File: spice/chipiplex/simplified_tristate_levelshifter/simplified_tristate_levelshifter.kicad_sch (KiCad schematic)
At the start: 24 parts, among them Q1 PNP, Q2 NPN, Q3 PNP, Q4 NPN

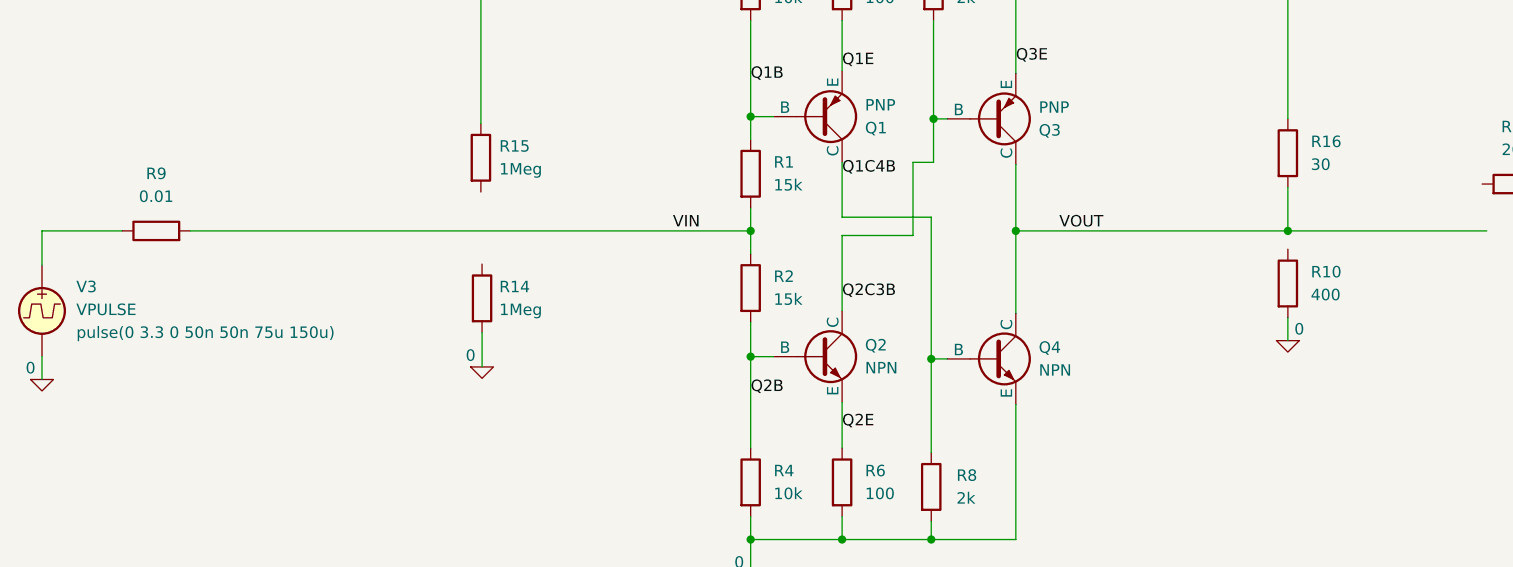
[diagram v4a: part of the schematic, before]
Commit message: Added finalized production files for v0.1r1.
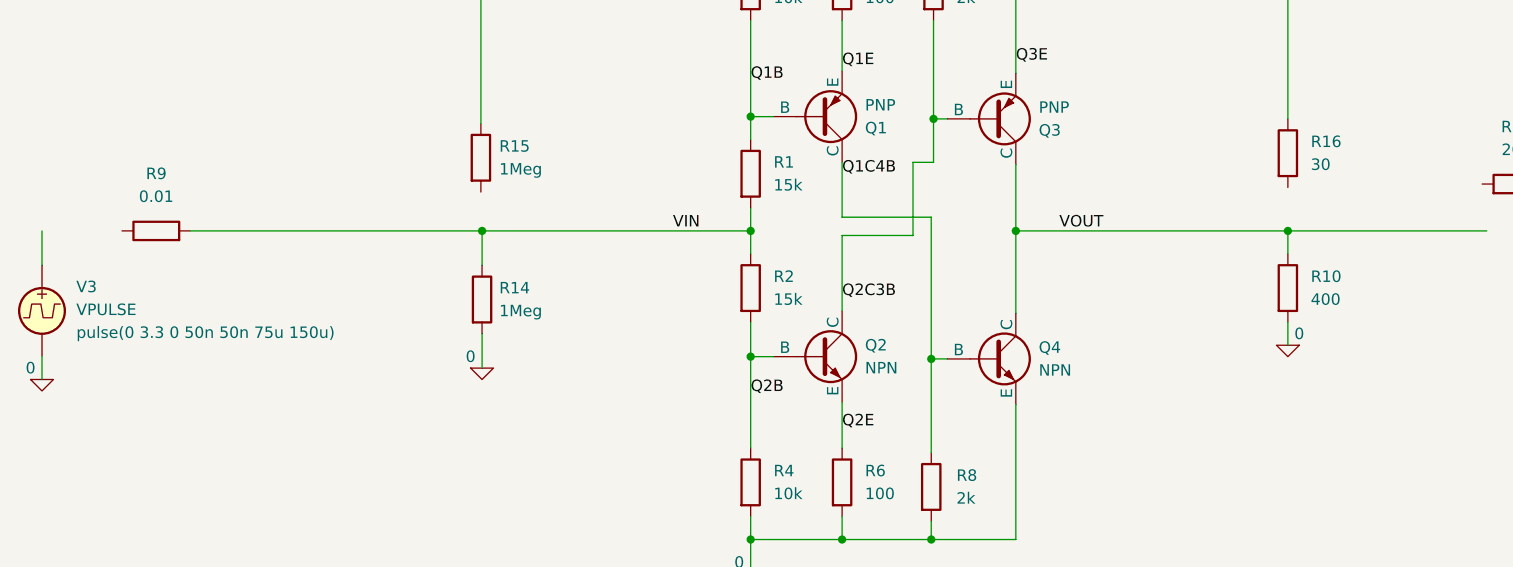
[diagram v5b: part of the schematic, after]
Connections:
- net VIN: now also R14.1
- net VOUT: now also R10.1; no longer R16.2
- net at R9.1: no longer V3.1
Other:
- moved on the sheet: R10
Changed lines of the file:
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@@
   (junction (at 124.206 130.81) (diameter 0) (color 0 0 0 0)
   )
+  (junction (at 133.604 96.52) (diameter 0) (color 0 0 0 0)
+  )
   (junction (at 163.83 96.52) (diameter 0) (color 0 0 0 0)
   )
-  (junction (at 133.604 96.52) (diameter 0) (color 0 0 0 0)
-  )
   (junction (at 104.14 96.52) (diameter 0) (color 0 0 0 0)
   )
@@
   (junction (at 124.206 110.744) (diameter 0) (color 0 0 0 0)
   )
+  (junction (at 74.295 96.52) (diameter 0) (color 0 0 0 0)
+  )
   (junction (at 114.3 130.81) (diameter 0) (color 0 0 0 0)
   )
@@
   (junction (at 104.267 62.738) (diameter 0) (color 0 0 0 0)
   )
+  (wire (pts (xy 74.295 96.52) (xy 104.14 96.52))
+    (stroke (width 0) (type default))
+  )
+  (wire (pts (xy 163.83 96.52) (xy 185.928 96.52))
+    (stroke (width 0) (type default))
+  )
   (wire (pts (xy 104.14 106.68) (xy 104.14 110.49))
     (stroke (width 0) (type default))
@@
     (stroke (width 0) (type default))
   )
-  (wire (pts (xy 74.295 107.823) (xy 74.295 111.633))
+  (wire (pts (xy 74.295 107.95) (xy 74.295 111.76))
     (stroke (width 0) (type default))
   )
@@
     (stroke (width 0) (type default))
   )
+  (wire (pts (xy 163.83 96.52) (xy 163.83 99.06))
+    (stroke (width 0) (type default))
+  )
   (wire (pts (xy 114.3 97.028) (xy 114.3 105.41))
     (stroke (width 0) (type default))
@@
     (stroke (width 0) (type default))
   )
+  (wire (pts (xy 74.295 96.52) (xy 74.295 100.33))
+    (stroke (width 0) (type default))
+  )
   (wire (pts (xy 133.604 115.824) (xy 133.604 130.81))
     (stroke (width 0) (type default))
@@
     (stroke (width 0) (type default))
   )
-  (wire (pts (xy 163.83 96.52) (xy 185.928 96.52))
-    (stroke (width 0) (type default))
-  )
-  (wire (pts (xy 41.91 96.52) (xy 104.14 96.52))
-    (stroke (width 0) (type default))
-  )
-  (wire (pts (xy 163.83 106.172) (xy 163.83 108.712))
-    (stroke (width 0) (type default))
-  )
-  (wire (pts (xy 25.4 96.52) (xy 34.29 96.52))
+  (wire (pts (xy 133.604 96.52) (xy 163.83 96.52))
+    (stroke (width 0) (type default))
+  )
+  (wire (pts (xy 41.91 96.52) (xy 74.295 96.52))
+    (stroke (width 0) (type default))
+  )
+  (wire (pts (xy 163.83 106.68) (xy 163.83 109.22))
     (stroke (width 0) (type default))
   )
@@
     (stroke (width 0) (type default))
   )
-  (wire (pts (xy 163.83 91.694) (xy 163.83 96.52))
-    (stroke (width 0) (type default))
-  )
   (wire (pts (xy 124.206 110.744) (xy 125.984 110.744))
     (stroke (width 0) (type default))
   )
   (wire (pts (xy 87.249 46.99) (xy 87.249 47.244))
-    (stroke (width 0) (type default))
-  )
-  (wire (pts (xy 133.604 96.52) (xy 163.83 96.52))
     (stroke (width 0) (type default))
   )
@@
     )
   )
-  (symbol (lib_id "Simulation_SPICE:0") (at 163.83 108.712 0) (mirror y) (unit 1)
+  (symbol (lib_id "Simulation_SPICE:0") (at 163.83 109.22 0) (mirror y) (unit 1)
     (in_bom yes) (on_board yes) (dnp no)
-    (property "Reference" "#GND05" (at 163.83 111.252 0)
-      (effects (font (size 1.27 1.27)) hide)
-    )
-    (property "Value" "0" (at 165.1 107.442 0)
-      (effects (font (size 1.27 1.27)))
-    )
-    (property "Footprint" "" (at 163.83 108.712 0)
-      (effects (font (size 1.27 1.27)) hide)
-    )
-    (property "Datasheet" "~" (at 163.83 108.712 0)
+    (property "Reference" "#GND05" (at 163.83 111.76 0)
+      (effects (font (size 1.27 1.27)) hide)
+    )
+    (property "Value" "0" (at 165.1 107.95 0)
+      (effects (font (size 1.27 1.27)))
+    )
+    (property "Footprint" "" (at 163.83 109.22 0)
+      (effects (font (size 1.27 1.27)) hide)
+    )
+    (property "Datasheet" "~" (at 163.83 109.22 0)
       (effects (font (size 1.27 1.27)) hide)
     )
@@
     )
   )
-  (symbol (lib_id "Simulation_SPICE:0") (at 74.295 111.633 0) (unit 1)
+  (symbol (lib_id "Simulation_SPICE:0") (at 74.295 111.76 0) (unit 1)
     (in_bom yes) (on_board yes) (dnp no)
-    (property "Reference" "#GND07" (at 74.295 114.173 0)
-      (effects (font (size 1.27 1.27)) hide)
-    )
-    (property "Value" "0" (at 73.025 110.363 0)
-      (effects (font (size 1.27 1.27)))
-    )
-    (property "Footprint" "" (at 74.295 111.633 0)
-      (effects (font (size 1.27 1.27)) hide)
-    )
-    (property "Datasheet" "~" (at 74.295 111.633 0)
+    (property "Reference" "#GND07" (at 74.295 114.3 0)
+      (effects (font (size 1.27 1.27)) hide)
+    )
+    (property "Value" "0" (at 73.025 110.49 0)
+      (effects (font (size 1.27 1.27)))
+    )
+    (property "Footprint" "" (at 74.295 111.76 0)
+      (effects (font (size 1.27 1.27)) hide)
+    )
+    (property "Datasheet" "~" (at 74.295 111.76 0)
       (effects (font (size 1.27 1.27)) hide)
     )
@@
     )
   )
-  (symbol (lib_id "Device:R") (at 163.83 102.362 0) (unit 1)
-    (in_bom yes) (on_board yes) (dnp no) (fields_autoplaced)
-    (property "Reference" "R10" (at 166.37 101.092 0)
-      (effects (font (size 1.27 1.27)) (justify left))
-    )
-    (property "Value" "400" (at 166.37 103.632 0)
-      (effects (font (size 1.27 1.27)) (justify left))
-    )
-    (property "Footprint" "" (at 162.052 102.362 90)
-      (effects (font (size 1.27 1.27)) hide)
-    )
-    (property "Datasheet" "~" (at 163.83 102.362 0)
+  (symbol (lib_id "Device:R") (at 163.83 102.87 0) (unit 1)
+    (in_bom yes) (on_board yes) (dnp no) (fields_autoplaced)
+    (property "Reference" "R10" (at 166.37 101.6 0)
+      (effects (font (size 1.27 1.27)) (justify left))
+    )
+    (property "Value" "400" (at 166.37 104.14 0)
+      (effects (font (size 1.27 1.27)) (justify left))
+    )
+    (property "Footprint" "" (at 162.052 102.87 90)
+      (effects (font (size 1.27 1.27)) hide)
+    )
+    (property "Datasheet" "~" (at 163.83 102.87 0)
       (effects (font (size 1.27 1.27)) hide)
     )
@@
     )
   )
-  (symbol (lib_id "Device:R") (at 74.295 104.013 0) (unit 1)
-    (in_bom yes) (on_board yes) (dnp no) (fields_autoplaced)
-    (property "Reference" "R14" (at 76.2 102.743 0)
-      (effects (font (size 1.27 1.27)) (justify left))
-    )
-    (property "Value" "1Meg" (at 76.2 105.283 0)
-      (effects (font (size 1.27 1.27)) (justify left))
-    )
-    (property "Footprint" "" (at 72.517 104.013 90)
-      (effects (font (size 1.27 1.27)) hide)
-    )
-    (property "Datasheet" "~" (at 74.295 104.013 0)
-      (effects (font (size 1.27 1.27)) hide)
-    )
+  (symbol (lib_id "Device:R") (at 74.295 104.14 0) (unit 1)
+    (in_bom yes) (on_board yes) (dnp no) (fields_autoplaced)
+    (property "Reference" "R14" (at 76.2 102.87 0)
+      (effects (font (size 1.27 1.27)) (justify left))
+    )
+    (property "Value" "1Meg" (at 76.2 105.41 0)
+      (effects (font (size 1.27 1.27)) (justify left))
+    )
+    (property "Footprint" "" (at 72.517 104.14 90)
+      (effects (font (size 1.27 1.27)) hide)
+    )
+    (property "Datasheet" "~" (at 74.295 104.14 0)
+      (effects (font (size 1.27 1.27)) hide)
+    )

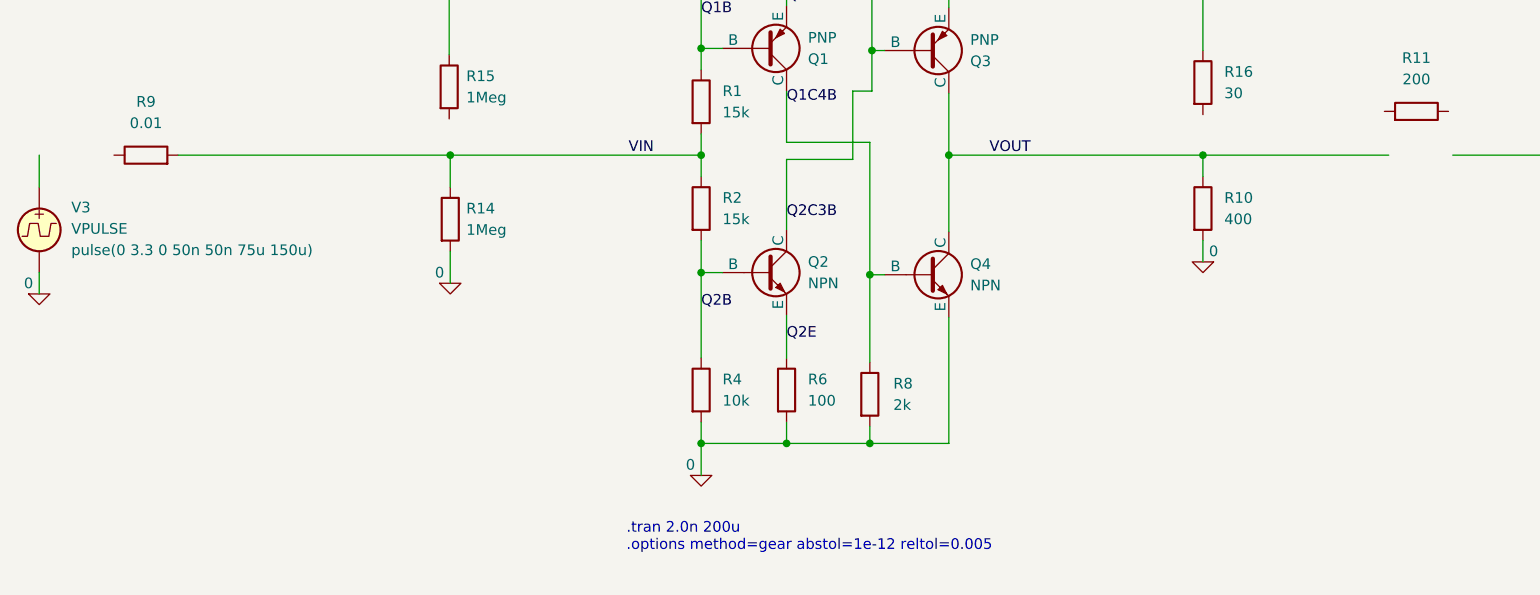
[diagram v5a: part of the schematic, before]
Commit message: Worked on spice models.
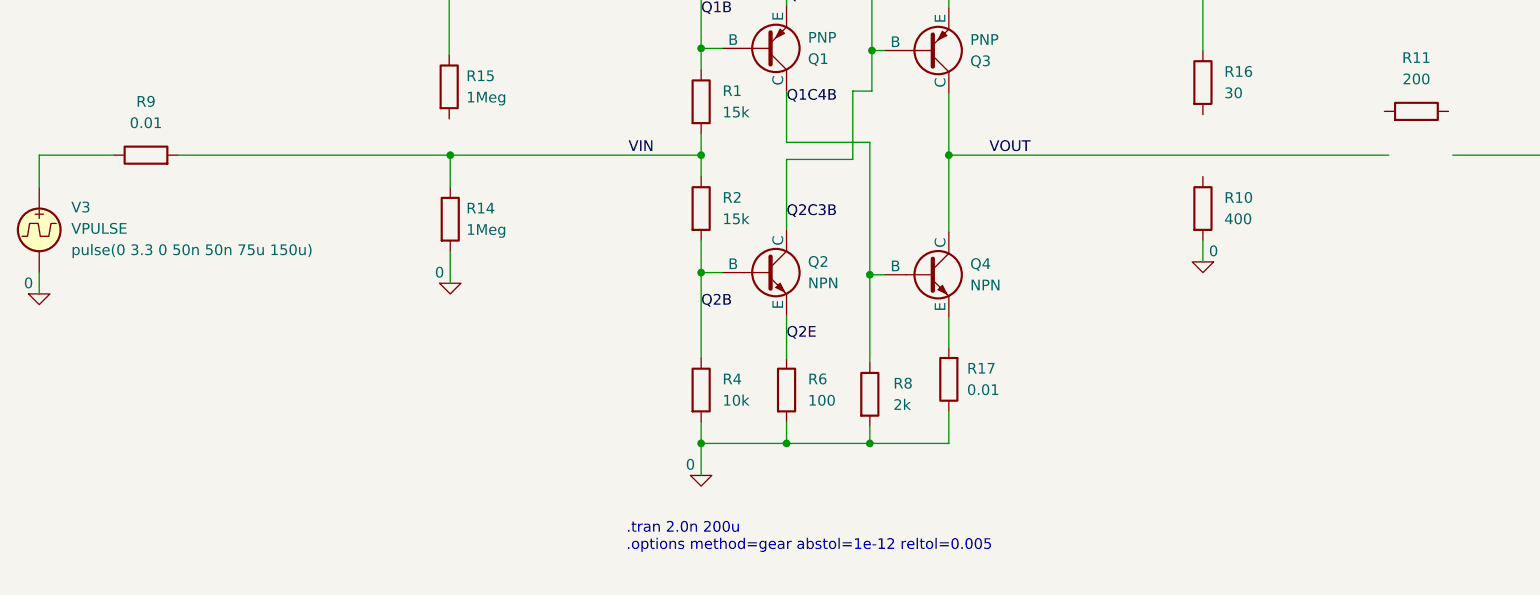
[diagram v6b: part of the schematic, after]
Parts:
- added R17: 0.01, symbol Device:R
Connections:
- net 0: now also R17.1; no longer Q4.3 (E)
- net VOUT: no longer R10.1
- net at R9.1: now also V3.1
- new net: Q4.3 (E), R17.2
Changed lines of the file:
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@@
   (junction (at 133.604 96.52) (diameter 0) (color 0 0 0 0)
   )
-  (junction (at 163.83 96.52) (diameter 0) (color 0 0 0 0)
-  )
   (junction (at 104.14 96.52) (diameter 0) (color 0 0 0 0)
   )
@@
     (stroke (width 0) (type default))
   )
-  (wire (pts (xy 163.83 96.52) (xy 185.928 96.52))
+  (wire (pts (xy 25.4 96.52) (xy 34.29 96.52))
     (stroke (width 0) (type default))
   )
@@
     (stroke (width 0) (type default))
   )
+  (wire (pts (xy 133.604 127) (xy 133.604 130.81))
+    (stroke (width 0) (type default))
+  )
   (wire (pts (xy 122.174 97.028) (xy 122.174 88.9))
     (stroke (width 0) (type default))
@@
     (stroke (width 0) (type default))
   )
-  (wire (pts (xy 163.83 96.52) (xy 163.83 99.06))
-    (stroke (width 0) (type default))
-  )
   (wire (pts (xy 114.3 97.028) (xy 114.3 105.41))
     (stroke (width 0) (type default))
@@
     (stroke (width 0) (type default))
   )
-  (wire (pts (xy 133.604 115.824) (xy 133.604 130.81))
-    (stroke (width 0) (type default))
-  )
   (wire (pts (xy 104.14 110.49) (xy 104.14 120.65))
     (stroke (width 0) (type default))
@@
     (stroke (width 0) (type default))
   )
+  (wire (pts (xy 133.604 115.824) (xy 133.604 119.38))
+    (stroke (width 0) (type default))
+  )
   (wire (pts (xy 114.3 94.996) (xy 124.206 94.996))
     (stroke (width 0) (type default))
@@
     (stroke (width 0) (type default))
   )
-  (wire (pts (xy 133.604 96.52) (xy 163.83 96.52))
+  (wire (pts (xy 133.604 96.52) (xy 185.928 96.52))
     (stroke (width 0) (type default))
   )
@@
         )
       )
+    )
+  )
+  (symbol (lib_id "Device:R") (at 133.604 123.19 180) (unit 1)
+    (in_bom yes) (on_board yes) (dnp no) (fields_autoplaced)
+    (property "Reference" "R17" (at 135.763 121.92 0)
+      (effects (font (size 1.27 1.27)) (justify right))
+    )
+    (property "Value" "0.01" (at 135.763 124.46 0)
+      (effects (font (size 1.27 1.27)) (justify right))
+    )
+    (property "Footprint" "" (at 135.382 123.19 90)
+      (effects (font (size 1.27 1.27)) hide)
+    )
+    (property "Datasheet" "~" (at 133.604 123.19 0)
+      (effects (font (size 1.27 1.27)) hide)
+    )
+    (pin "1")
+    (pin "2")
+    (instances
+      (project "simplified_tristate_levelshifter"
+        (path "/971ad994-0ee5-4437-b2dc-8f417495b480"
+          (reference "R17") (unit 1)
+        )
+      )
